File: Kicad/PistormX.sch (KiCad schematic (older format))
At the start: 20 parts, among them J1 68000D socket, J2 Raspberry_Pi_2_3, J3 PROG, U1 XC95144XL-TQ100, U2 SPX3819M5-L-3-3, U3 XC6206PxxxMR

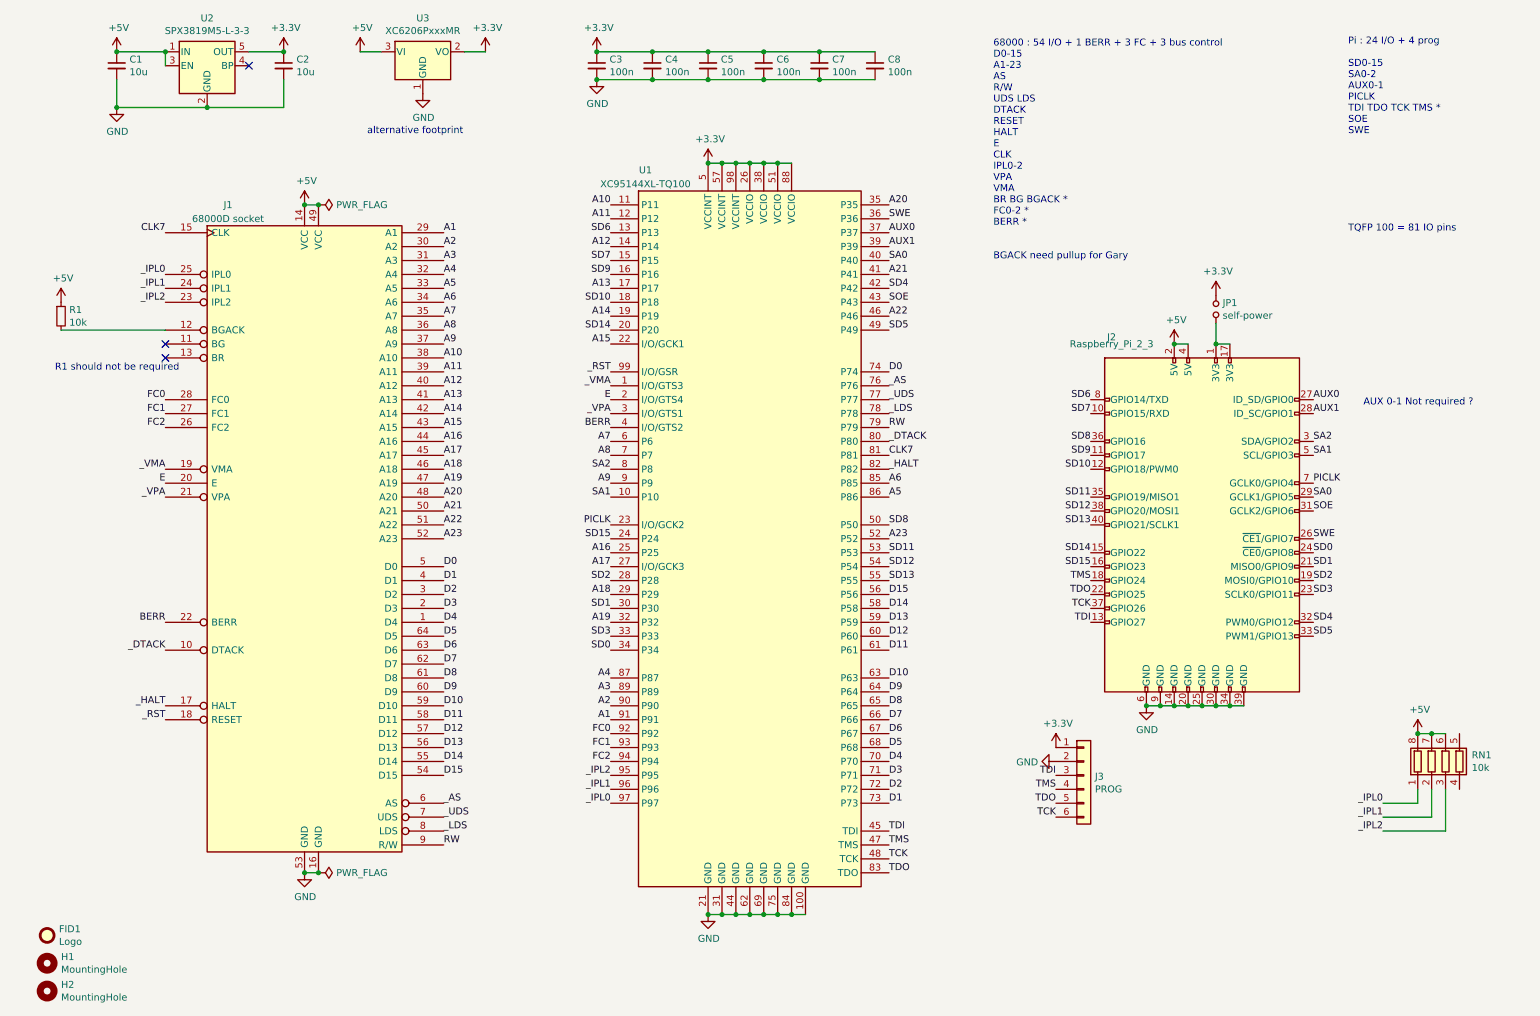
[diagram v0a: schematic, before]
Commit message: Kicad : first board revision ; CPLD : working with buptest and emulator, no 200MHz PICLK is used, fixed cold and warm reset
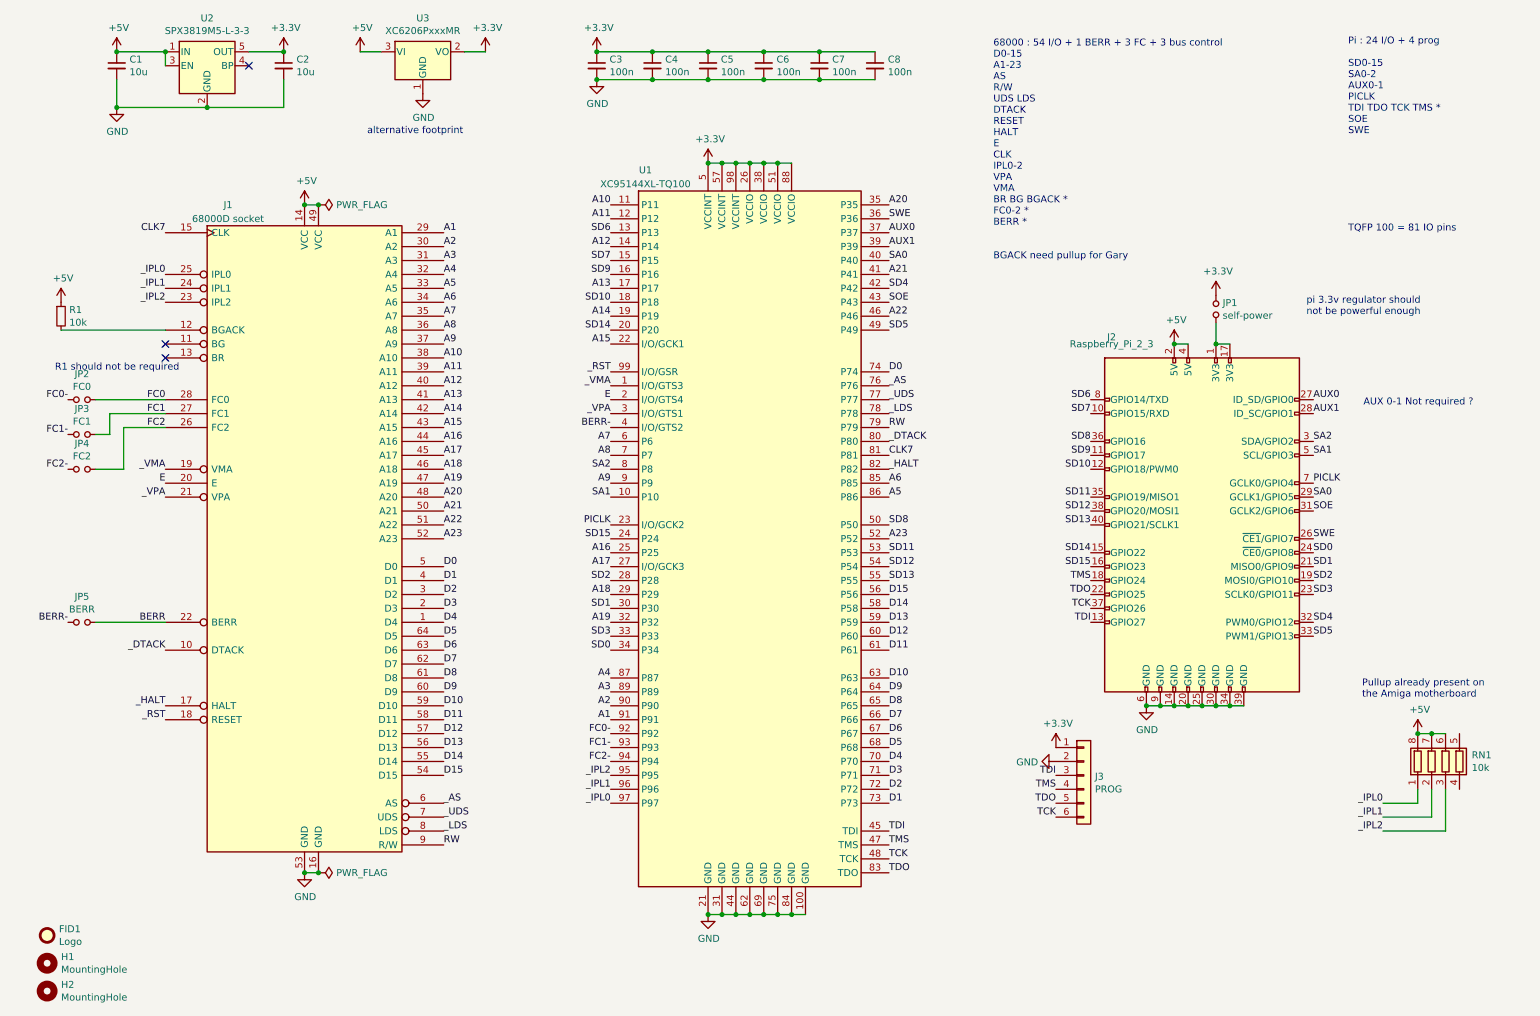
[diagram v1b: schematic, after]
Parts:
- added JP2: FC0, Jumper:SolderJumper-2_P1.3mm_Open_RoundedPad1.0x1.5mm, symbol Device:Jumper_NO_Small
- added JP3: FC1, Jumper:SolderJumper-2_P1.3mm_Open_RoundedPad1.0x1.5mm, symbol Device:Jumper_NO_Small
- added JP4: FC2, Jumper:SolderJumper-2_P1.3mm_Open_RoundedPad1.0x1.5mm, symbol Device:Jumper_NO_Small
- added JP5: BERR, Jumper:SolderJumper-2_P1.3mm_Open_RoundedPad1.0x1.5mm, symbol Device:Jumper_NO_Small
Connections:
- net BERR: now also JP5.2; no longer U1.4 (I/O/GTS2)
- net FC0: now also JP2.2; no longer U1.92 (P92)
- net FC1: now also JP3.2; no longer U1.93 (P93)
- net FC2: now also JP4.2; no longer U1.94 (P94)
- new net BERR-: JP5.1, U1.4 (I/O/GTS2)
- new net FC0-: JP2.1, U1.92 (P92)
- new net FC1-: JP3.1, U1.93 (P93)
- new net FC2-: JP4.1, U1.94 (P94)
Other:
- note added: "Pullup already present on\nthe Amiga motherboard"
- note added: "pi 3.3v regulator should\nnot be powerful enough"
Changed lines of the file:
@@
 Text Label 1500 4950 2    50   ~ 0
-BERR
-Text Label 4700 5750 2    50   ~ 0
-FC0
-Text Label 4700 5850 2    50   ~ 0
-FC1
-Text Label 4700 5950 2    50   ~ 0
-FC2
-Text Label 4700 3550 2    50   ~ 0
 BERR
 $Comp
@@
 	1    0    0    -1
 $EndComp
+$Comp
+L Device:Jumper_NO_Small JP5
+U 1 1 618C0E0C
+P 900 4950
+F 0 "JP5" H 900 5135 50  0000 C CNN
+F 1 "BERR" H 900 5044 50  0000 C CNN
+F 2 "Jumper:SolderJumper-2_P1.3mm_Open_RoundedPad1.0x1.5mm" H 900 4950 50  0001 C CNN
+F 3 "~" H 900 4950 50  0001 C CNN
+	1    900  4950
+	1    0    0    -1
+$EndComp
+$Comp
+L Device:Jumper_NO_Small JP2
+U 1 1 618C5E3E
+P 900 3350
+F 0 "JP2" H 900 3535 50  0000 C CNN
+F 1 "FC0" H 900 3444 50  0000 C CNN
+F 2 "Jumper:SolderJumper-2_P1.3mm_Open_RoundedPad1.0x1.5mm" H 900 3350 50  0001 C CNN
+F 3 "~" H 900 3350 50  0001 C CNN
+	1    900  3350
+	1    0    0    -1
+$EndComp
+$Comp
+L Device:Jumper_NO_Small JP3
+U 1 1 618C6B4D
+P 900 3600
+F 0 "JP3" H 900 3785 50  0000 C CNN
+F 1 "FC1" H 900 3694 50  0000 C CNN
+F 2 "Jumper:SolderJumper-2_P1.3mm_Open_RoundedPad1.0x1.5mm" H 900 3600 50  0001 C CNN
+F 3 "~" H 900 3600 50  0001 C CNN
+	1    900  3600
+	1    0    0    -1
+$EndComp
+$Comp
+L Device:Jumper_NO_Small JP4
+U 1 1 618C6EFB
+P 900 3850
+F 0 "JP4" H 900 4035 50  0000 C CNN
+F 1 "FC2" H 900 3944 50  0000 C CNN
+F 2 "Jumper:SolderJumper-2_P1.3mm_Open_RoundedPad1.0x1.5mm" H 900 3850 50  0001 C CNN
+F 3 "~" H 900 3850 50  0001 C CNN
+	1    900  3850
+	1    0    0    -1
+$EndComp
+Text Label 800  3350 2    50   ~ 0
+FC0-
+Text Label 800  3600 2    50   ~ 0
+FC1-
+Text Label 800  3850 2    50   ~ 0
+FC2-
+Wire Wire Line
+	1500 3350 1000 3350
+Wire Wire Line
+	1500 3450 1100 3450
+Wire Wire Line
+	1100 3450 1100 3600
+Wire Wire Line
+	1100 3600 1000 3600
+Wire Wire Line
+	1500 3550 1200 3550
+Wire Wire Line
+	1200 3550 1200 3850
+Wire Wire Line
+	1200 3850 1000 3850
+Wire Wire Line
+	1500 4950 1000 4950
+Text Label 800  4950 2    50   ~ 0
+BERR-
+Text Label 4700 3550 2    50   ~ 0
+BERR-
+Text Label 4700 5950 2    50   ~ 0
+FC2-
+Text Label 4700 5850 2    50   ~ 0
+FC1-
+Text Label 4700 5750 2    50   ~ 0
+FC0-
+Text Notes 10100 5500 0    50   ~ 0
+Pullup already present on\nthe Amiga motherboard
+Text Notes 9700 2750 0    50   ~ 0
+pi 3.3v regulator should\nnot be powerful enough
 $EndSCHEMATC
